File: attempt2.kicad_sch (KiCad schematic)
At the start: 71 parts, among them J1 SIM_Card, J3 U.FL-R-SMT-110, J4 USB_C_Receptacle_USB2.0_14P, J5 U.FL-R-SMT-110, SW3 SW_Push, SW4 SW_Push, U1 nRF9160-SIxA, U2 TPD3F303DPVR, U3 MCP73831T-2ACI_OT, U4 MIC94092YC6-TR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

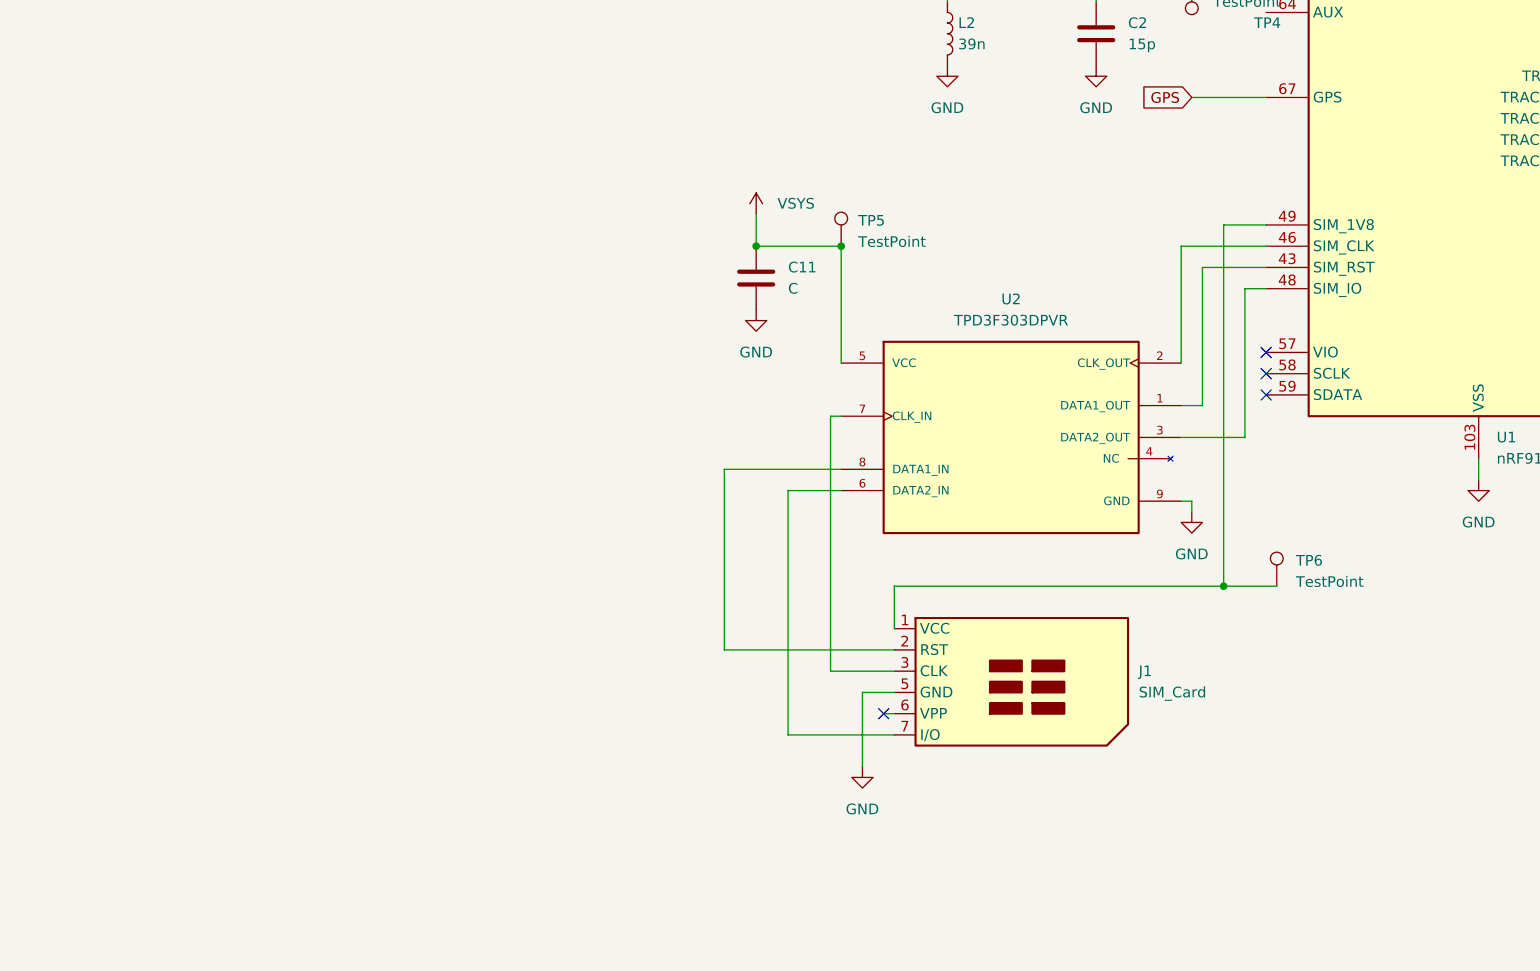
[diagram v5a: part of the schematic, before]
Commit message: switched to an esim
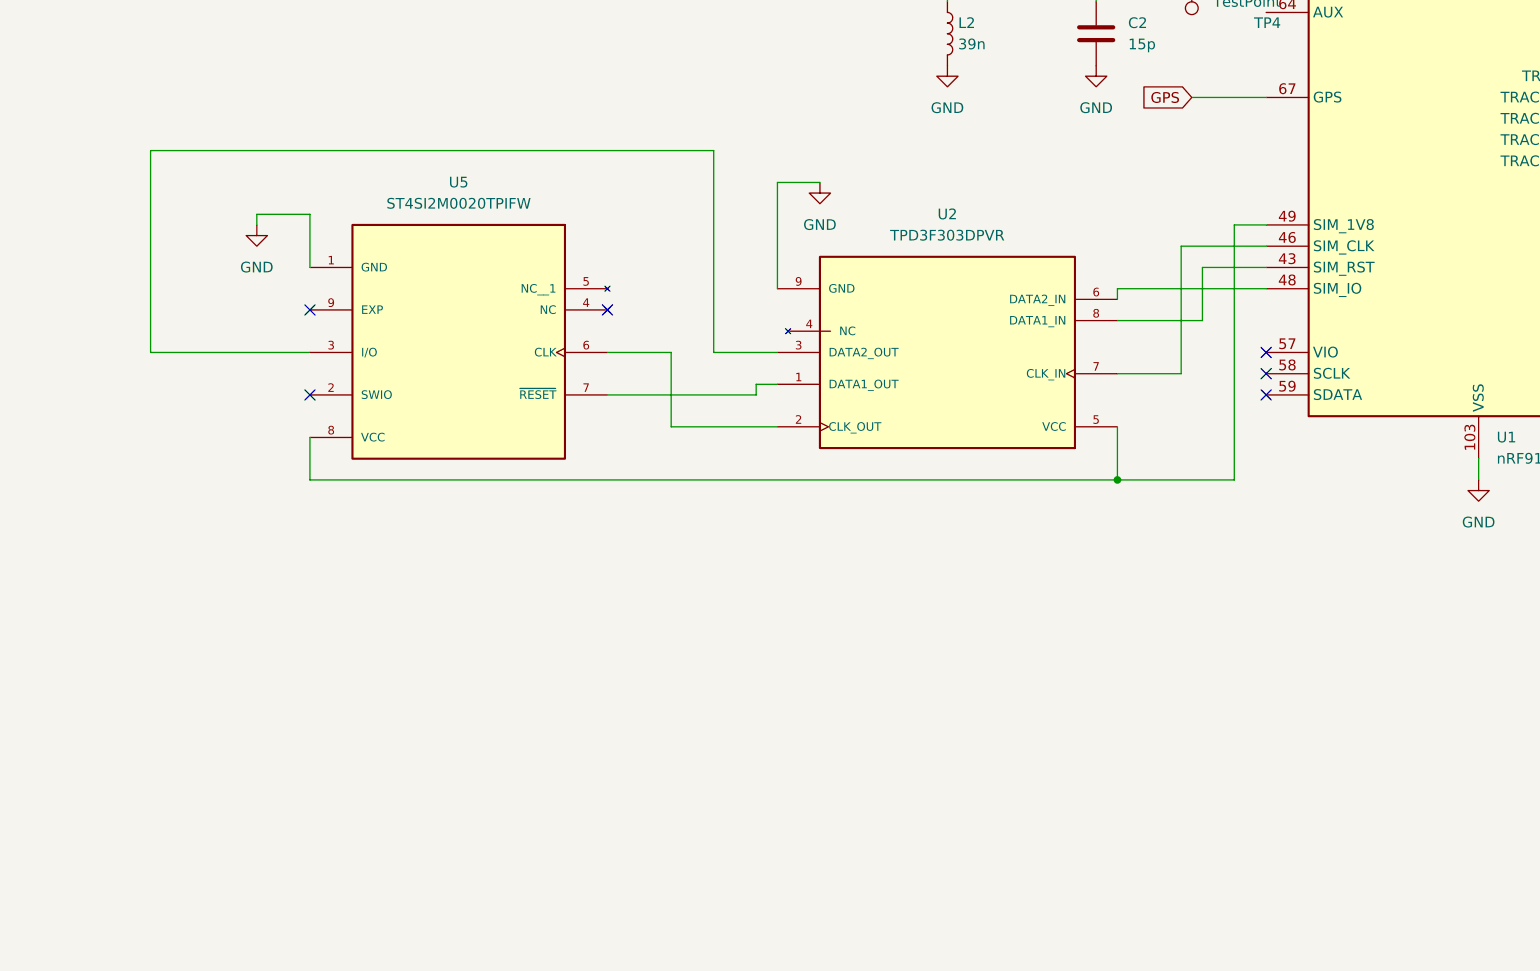
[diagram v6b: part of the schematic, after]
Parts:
- removed C11: C, Capacitor_SMD:C_1206_3216Metric, symbol Device:C
- removed J1: SIM_Card, Connector_Card:nanoSIM_GCT_SIM8060-6-1-14-00, symbol Connector:SIM_Card
- removed TP5, TP6: TestPoint, TestPoint:TestPoint_Pad_D2.0mm, symbol Connector:TestPoint
- added U5: ST4SI2M0020TPIFW, ST4SI2M0020TPIFW:SON127P500X600X100-9N, symbol ST4SI2M0020TPIFW:ST4SI2M0020TPIFW
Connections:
- net GND: now also U5.1 (GND)
- net VSYS: no longer U2.5 (VCC)
- net at U2.1 (DATA1_OUT): now also U5.7 (~{RESET}); no longer U1.43 (SIM_RST)
- net at U2.2 (CLK_OUT): now also U5.6 (CLK); no longer U1.46 (SIM_CLK)
- net at U2.3 (DATA2_OUT): now also U5.3 (I/O); no longer U1.48 (SIM_IO)
- net at U2.6 (DATA2_IN): now also U1.48 (SIM_IO)
- net at U2.7 (CLK_IN): now also U1.46 (SIM_CLK)
- net at U2.8 (DATA1_IN): now also U1.43 (SIM_RST)
- net at U1.49 (SIM_1V8): now also U2.5 (VCC), U5.8 (VCC)
- no-connect marks 49 -> 51
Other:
- moved on the sheet: U2
